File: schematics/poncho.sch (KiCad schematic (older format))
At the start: 11 parts, among them P1 CONN_20X2, P2 CONN_20X2

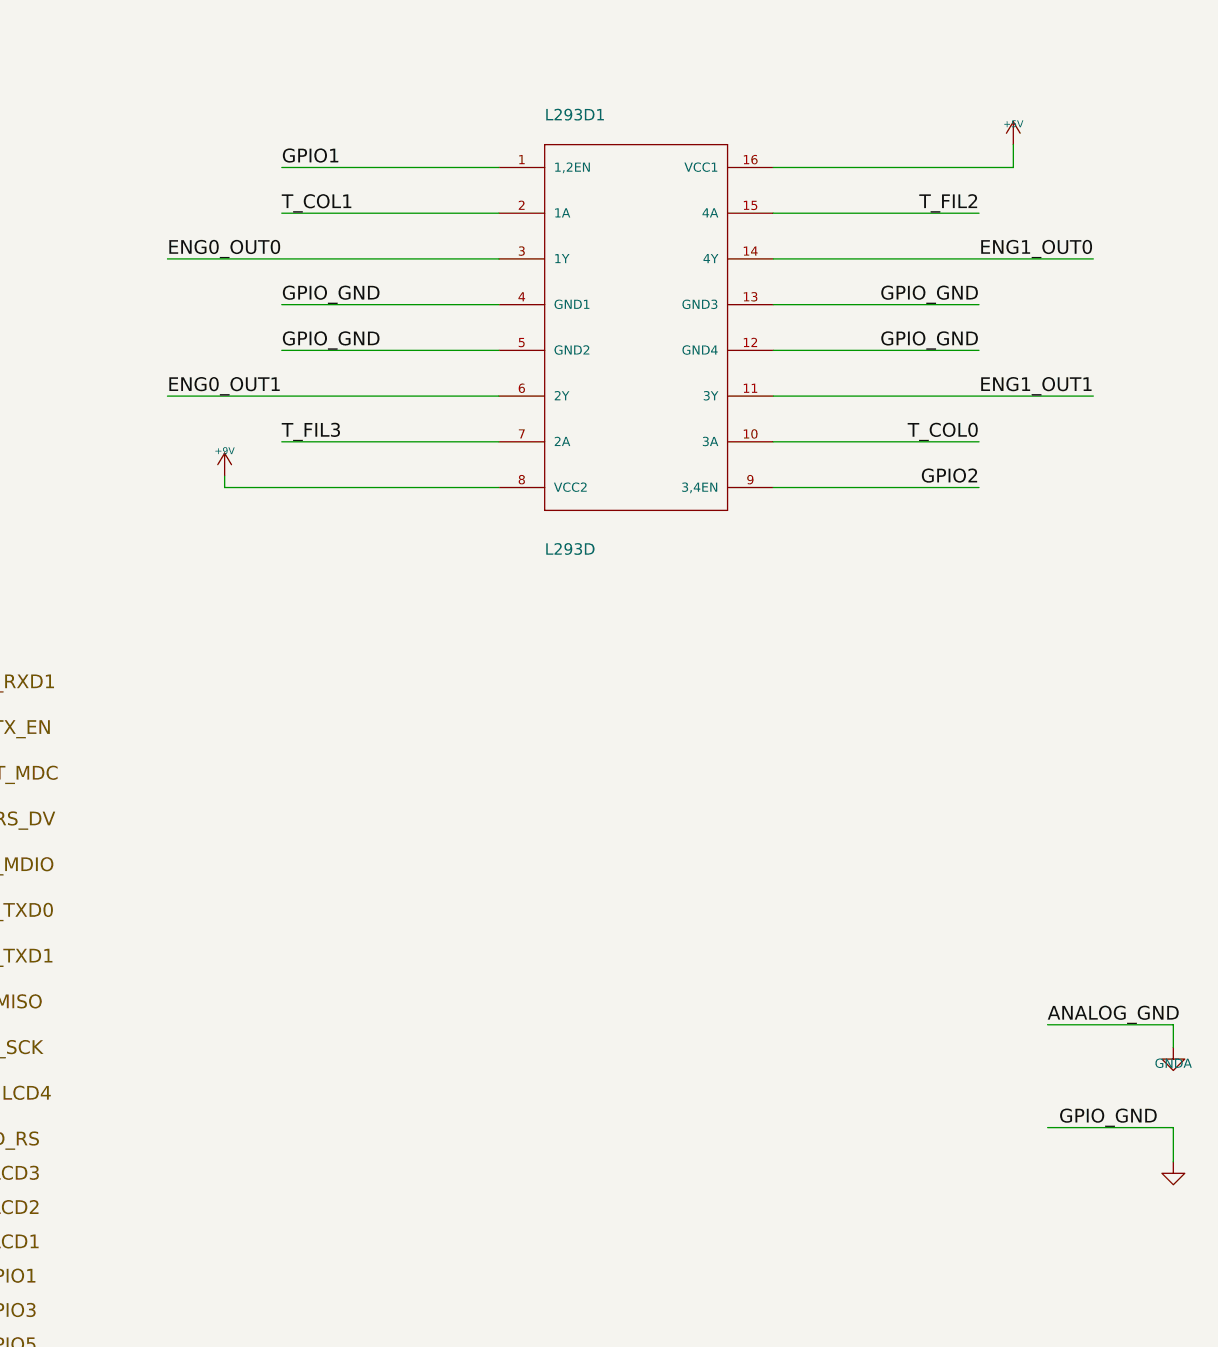
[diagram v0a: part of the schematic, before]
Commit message: Se agregaron modificaciones en los labels del .sch. [TODO] Averiguar como relacionar los resistores con su footprint correspontiente.
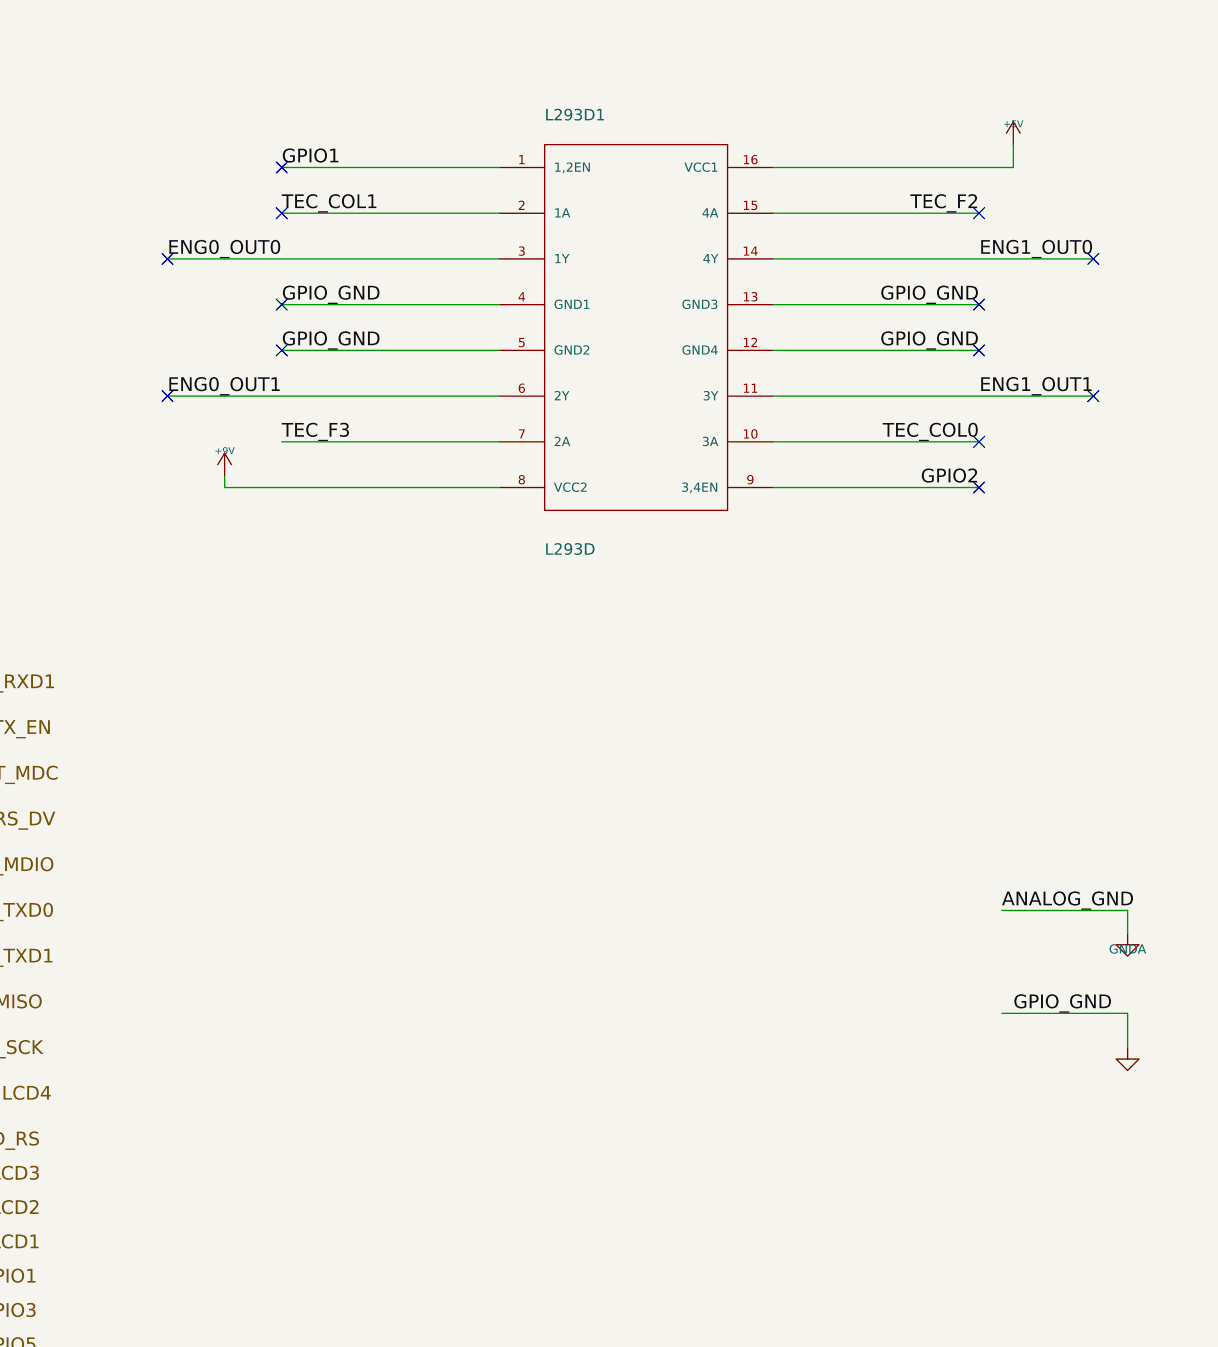
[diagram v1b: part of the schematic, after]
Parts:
- L293D1: footprint stepper drivers-DIL16 -> Housings_DIP:DIP-16_W7.62mm
- P1, P2: footprint (none) -> Pin_Headers:Pin_Header_Straight_2x20
- R20, R21, R22, R23: footprint SM0805 -> Resistors_ThroughHole:Resistor_Cement_Horizontal_Meggitt-SBC-2
- TH1, TH2, TH3, TH4: footprint MF-MSMF -> Discret:R1
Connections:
- net labels removed: T_COL0, T_COL1, T_FIL2, T_FIL3
- no-connect marks 0 -> 13
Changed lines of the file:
@@
 LIBS:stepper drivers
 LIBS:poncho-cache
-EELAYER 27 0
+EELAYER 25 0
 EELAYER END
 $Descr A4 11693 8268
 encoding utf-8
 Sheet 1 1
-Title "GPIO"
-Date "29 sep 2015"
+Title "Poncho de control de motores por Wi-Fi"
+Date "jue 01 oct 2015"
 Rev "1.1"
 Comp ""
@@
 F 0 "L293D1" H 8100 3800 50  0000 L BNN
 F 1 "L293D" H 8100 1900 50  0000 L BNN
-F 2 "stepper drivers-DIL16" H 8500 3050 50  0001 C CNN
+F 2 "Housings_DIP:DIP-16_W7.62mm" H 8500 3050 50  0001 C CNN
 F 3 "" H 8500 2900 60  0000 C CNN
 	1    8500 2900
@@
 GPIO2
 Text Label 6950 2400 0    60   ~ 0
-T_COL1
+TEC_COL1
 Text Label 6950 3400 0    60   ~ 0
-T_FIL3
+TEC_F3
 Text Label 10000 2400 2    60   ~ 0
-T_FIL2
+TEC_F2
 Text Label 6450 2600 0    60   ~ 0
 ENG0_OUT0
@@
 F 0 "TH1" V 2550 1100 50  0000 C CNN
 F 1 "MF-MSMF030-2" V 2350 1050 50  0000 C CNN
-F 2 "MF-MSMF" H 2450 1050 60  0001 C CNN
+F 2 "Discret:R1" H 2450 1050 60  0001 C CNN
 F 3 "mfmsmf.pdf" H 2450 1050 60  0001 C CNN
 F 4 "PTC RESETTABLE .30A 30V 1812" V 2450 1050 60  0001 C CNN "Descripción"
@@
 L GNDA #PWR04
 U 1 1 52DEB0D0
-P 10850 6050
-F 0 "#PWR04" H 10850 6050 40  0001 C CNN
-F 1 "GNDA" H 10850 5980 40  0000 C CNN
-F 2 "" H 10850 6050 60  0000 C CNN
-F 3 "" H 10850 6050 60  0000 C CNN
-	1    10850 6050
+P 10650 5550
+F 0 "#PWR04" H 10650 5550 40  0001 C CNN
+F 1 "GNDA" H 10650 5480 40  0000 C CNN
+F 2 "" H 10650 5550 60  0000 C CNN
+F 3 "" H 10650 5550 60  0000 C CNN
+	1    10650 5550
 	1    0    0    -1
 $EndComp
@@
 F 0 "TH2" V 3550 1100 50  0000 C CNN
 F 1 "MF-MSMF030-2" V 3350 1050 50  0000 C CNN
-F 2 "MF-MSMF" H 2450 1050 60  0001 C CNN
+F 2 "Discret:R1" H 2450 1050 60  0001 C CNN
 F 3 "mfmsmf.pdf" H 2450 1050 60  0001 C CNN
 F 4 "PTC RESETTABLE .30A 30V 1812" V 2450 1050 60  0001 C CNN "Descripción"
@@
 F 0 "P1" H 2950 3450 60  0000 C CNN
 F 1 "CONN_20X2" V 2950 2400 50  0000 C CNN
-F 2 "" H 2950 2400 60  0000 C CNN
+F 2 "Pin_Headers:Pin_Header_Straight_2x20" H 2950 2400 60  0001 C CNN
 F 3 "" H 2950 2400 60  0000 C CNN
 	1    2950 2400
@@
 F 0 "P2" H 3400 7250 60  0000 C CNN
 F 1 "CONN_20X2" V 3400 6200 50  0000 C CNN
-F 2 "" H 3400 6200 60  0000 C CNN
+F 2 "Pin_Headers:Pin_Header_Straight_2x20" H 3400 6200 60  0001 C CNN
 F 3 "" H 3400 6200 60  0000 C CNN
 	1    3400 6200
@@
 F 0 "R20" V 1780 1700 40  0000 C CNN
 F 1 "470" V 1707 1701 40  0000 C CNN
-F 2 "SM0805" V 1630 1700 30  0001 C CNN
+F 2 "Resistors_ThroughHole:Resistor_Cement_Horizontal_Meggitt-SBC-2" V 1630 1700 30  0001 C CNN
 F 3 "AOA0000CE1.pdf" H 1700 1700 30  0001 C CNN
 F 4 "RES 470 OHM 1/8W 5% 0805 SMD" V 1700 1700 60  0001 C CNN "Descripción"
@@
 F 0 "R21" V 1780 1500 40  0000 C CNN
 F 1 "1k2" V 1707 1501 40  0000 C CNN
-F 2 "SM0805" V 1630 1500 30  0001 C CNN
+F 2 "Resistors_ThroughHole:Resistor_Cement_Horizontal_Meggitt-SBC-2" V 1630 1500 30  0001 C CNN
 F 3 "SEI-RMCF_RMCP.pdf" H 1700 1500 30  0001 C CNN
 F 4 "RES 1.2K OHM 1/8W 5% 0805" V 1700 1500 60  0001 C CNN "Descripción"
@@
 F 0 "R22" V 1780 1300 40  0000 C CNN
 F 1 "1k2" V 1707 1301 40  0000 C CNN
-F 2 "SM0805" V 1630 1500 30  0001 C CNN
+F 2 "Resistors_ThroughHole:Resistor_Cement_Horizontal_Meggitt-SBC-2" V 1630 1500 30  0001 C CNN
 F 3 "SEI-RMCF_RMCP.pdf" H 1700 1500 30  0001 C CNN
 F 4 "RES 1.2K OHM 1/8W 5% 0805" V 1700 1500 60  0001 C CNN "Descripción"
@@
 F 0 "R23" V 1780 1100 40  0000 C CNN
 F 1 "1k2" V 1707 1101 40  0000 C CNN
-F 2 "SM0805" V 1630 1500 30  0001 C CNN
+F 2 "Resistors_ThroughHole:Resistor_Cement_Horizontal_Meggitt-SBC-2" V 1630 1500 30  0001 C CNN
 F 3 "SEI-RMCF_RMCP.pdf" H 1700 1500 30  0001 C CNN
 F 4 "RES 1.2K OHM 1/8W 5% 0805" V 1700 1500 60  0001 C CNN "Descripción"
@@
 F 0 "TH3" V 3000 4900 50  0000 C CNN
 F 1 "MF-MSMF030-2" V 2800 4850 50  0000 C CNN
-F 2 "MF-MSMF" H -2450 4850 60  0001 C CNN
+F 2 "Discret:R1" H -2450 4850 60  0001 C CNN
 F 3 "mfmsmf.pdf" H -2450 4850 60  0001 C CNN
 F 4 "PTC RESETTABLE .30A 30V 1812" V -2450 4850 60  0001 C CNN "Descripción"
@@
 F 0 "TH4" V 4000 4900 50  0000 C CNN
 F 1 "MF-MSMF030-2" V 3800 4850 50  0000 C CNN
-F 2 "MF-MSMF" H -2450 4850 60  0001 C CNN
+F 2 "Discret:R1" H -2450 4850 60  0001 C CNN
 F 3 "mfmsmf.pdf" H -2450 4850 60  0001 C CNN
 F 4 "PTC RESETTABLE .30A 30V 1812" V -2450 4850 60  0001 C CNN "Descripción"
@@
 L GND #PWR08
 U 1 1 53B8B104
-P 10850 6550
-F 0 "#PWR08" H 10850 6550 30  0001 C CNN
-F 1 "GND" H 10850 6480 30  0001 C CNN
-F 2 "" H 10850 6550 60  0000 C CNN
-F 3 "" H 10850 6550 60  0000 C CNN
-	1    10850 6550
-	1    0    0    -1
-$EndComp
-Text Label 10350 6400 0    60   ~ 0
+P 10650 6050
+F 0 "#PWR08" H 10650 6050 30  0001 C CNN
+F 1 "GND" H 10650 5980 30  0001 C CNN
+F 2 "" H 10650 6050 60  0000 C CNN
+F 3 "" H 10650 6050 60  0000 C CNN
+	1    10650 6050
+	1    0    0    -1
+$EndComp
+Text Label 10150 5900 0    60   ~ 0
 GPIO_GND
 Text Label 750  5050 0    60   ~ 0
@@
 Text Label 4700 2550 0    60   ~ 0
 GPIO_GND
-Text Label 10300 5950 0    60   ~ 0
+Text Label 10100 5450 0    60   ~ 0
 ANALOG_GND
 Text Label 4550 1950 0    60   ~ 0
@@
 	2200 900  2200 1750
 Wire Wire Line
-	10850 5950 10300 5950
-Wire Wire Line
-	10850 6050 10850 5950
+	10650 5450 10100 5450
+Wire Wire Line
+	10650 5550 10650 5450
 Wire Wire Line
 	950  750  2250 750
@@
 	5150 6350 5150 6450
 Wire Wire Line
-	10850 6400 10300 6400
-Wire Wire Line
-	10850 6550 10850 6400
+	10650 5900 10100 5900
+Wire Wire Line
+	10650 6050 10650 5900
 Wire Wire Line
 	750  4250 2600 4250
@@
 	1100 1900 1950 1900
 Text Label 10000 3400 2    60   ~ 0
-T_COL0
+TEC_COL0
+NoConn ~ 6450 2600
+NoConn ~ 6450 3200
+NoConn ~ 6950 2800
+NoConn ~ 6950 3000
+NoConn ~ 6950 2200
+NoConn ~ 6950 2400
+NoConn ~ 10000 2400
+NoConn ~ 10500 2600
+NoConn ~ 10000 2800
+NoConn ~ 10000 3000
+NoConn ~ 10500 3200
+NoConn ~ 10000 3400
+NoConn ~ 10000 3600
 $EndSCHEMATC

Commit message: Esquemático parcialmente terminado. [TODO] PCB.
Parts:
- removed R20: 470, Resistors_ThroughHole:Resistor_Cement_Horizontal_Meggitt-SBC-2, symbol R
- removed R21, R22, R23: 1k2, Resistors_ThroughHole:Resistor_Cement_Horizontal_Meggitt-SBC-2, symbol R
- removed TH1, TH2, TH3, TH4: MF-MSMF030-2, Discret:R1, symbol THERMISTOR
- added P3: ESP8266, Housings_DIP:DIP-8_W7.62mm_LongPads, symbol DIL8
- L293D1: footprint Housings_DIP:DIP-16_W7.62mm -> Housings_DIP:DIP-16_W7.62mm_LongPads
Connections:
- wire segments 258 -> 261
- no-connect marks 13 -> 4
